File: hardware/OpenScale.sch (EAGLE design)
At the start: 64 parts, among them Q1 200mA/50V, Q2 200mA/50V, Q3 MMBT4403, U1 HX711, U3 TMP102, U4 ATMEGA328P_TQFP, U6 FT231X, Y2 16MHZ

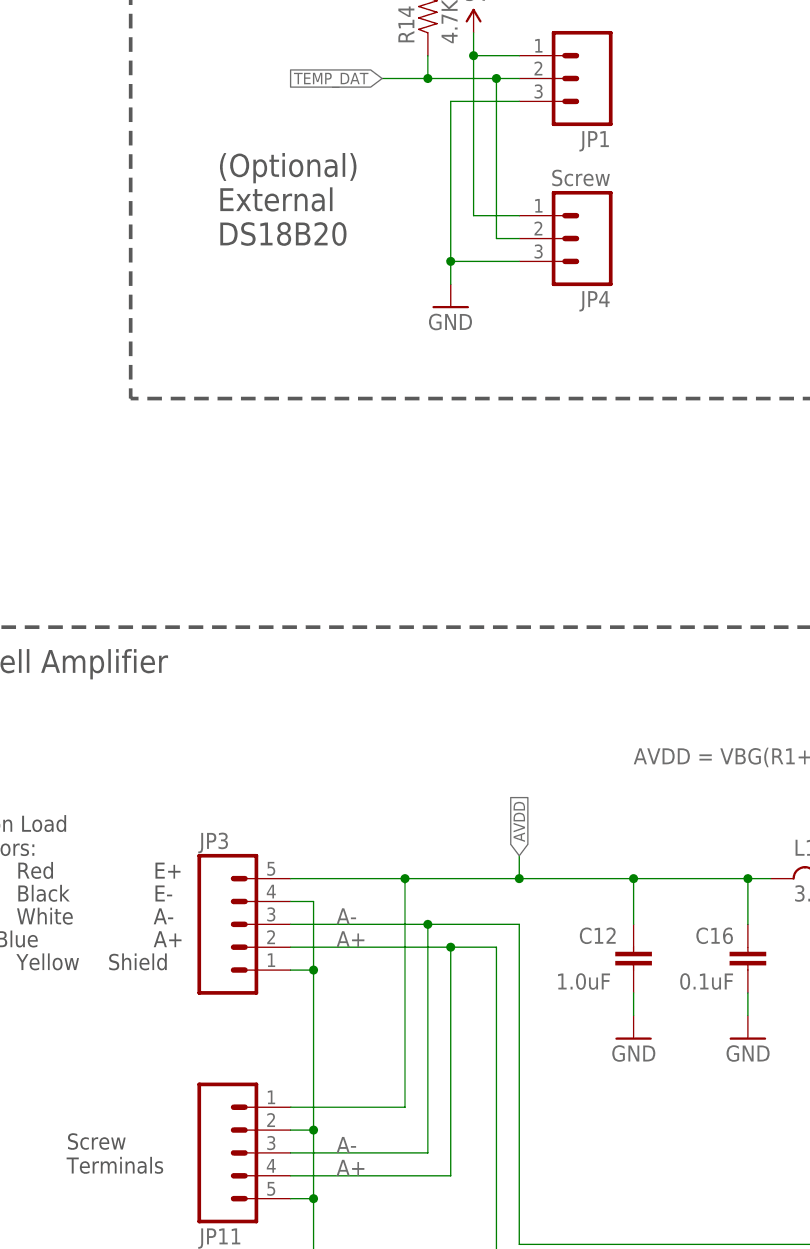
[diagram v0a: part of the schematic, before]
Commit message: Value Additions to .brd and .sch for 3D Model
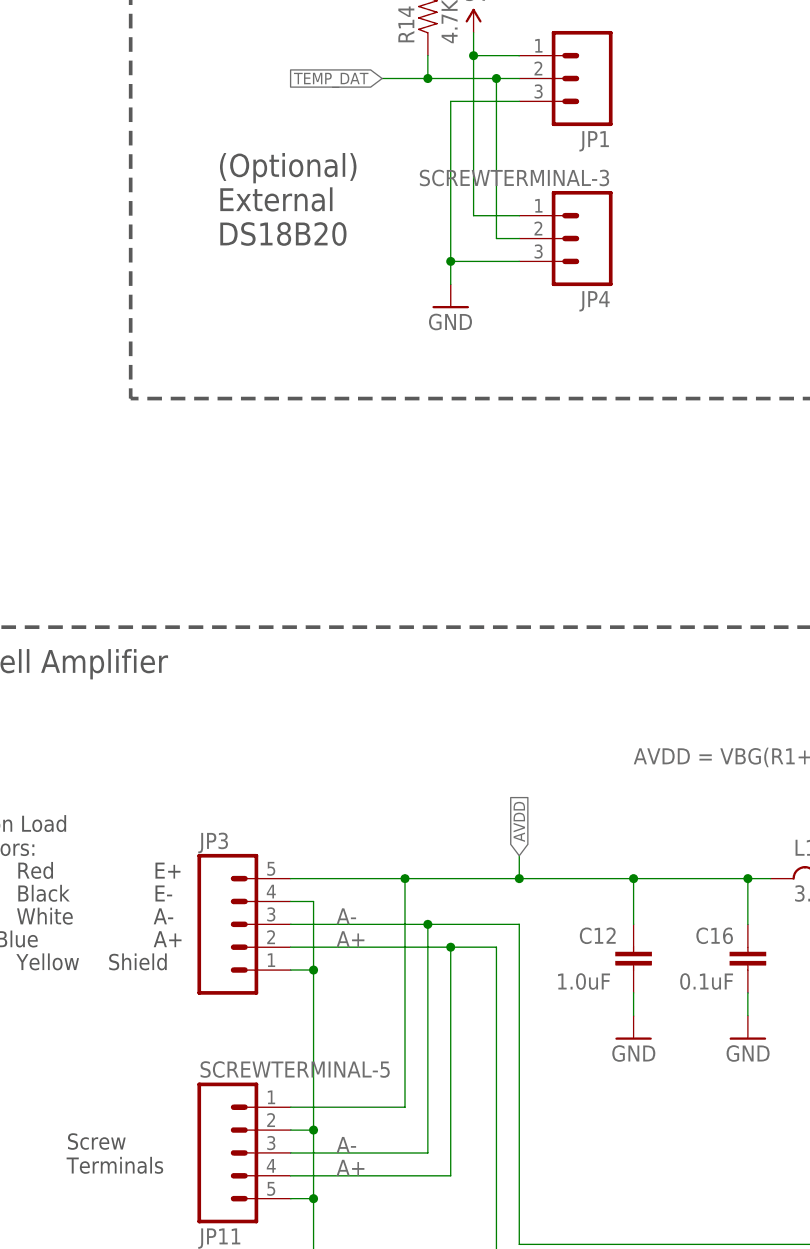
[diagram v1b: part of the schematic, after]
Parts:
- JP11: value (none) -> SCREWTERMINAL-5
- JP4: value Screw -> SCREWTERMINAL-3
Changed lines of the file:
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@@
 <?xml version="1.0" encoding="utf-8"?>
 <!DOCTYPE eagle SYSTEM "eagle.dtd">
-<eagle version="7.1.0">
+<eagle version="7.2.0">
 <drawing>
 <settings>
@@
 <part name="GND20" library="SparkFun-Aesthetics" deviceset="GND" device=""/>
 <part name="LOGO3" library="SparkFun-Aesthetics" deviceset="SFE_LOGO_FLAME" device=".1_STOP" value="SFE_LOGO_FLAME.1_STOP"/>
-<part name="JP4" library="SparkFun-Connectors" deviceset="M03" device="SCREW_LOCK" value="Screw"/>
+<part name="JP4" library="SparkFun-Connectors" deviceset="M03" device="SCREW_LOCK" value="SCREWTERMINAL-3"/>
 <part name="JP3" library="SparkFun-Connectors" deviceset="M05" device="NO_SILK"/>
-<part name="JP11" library="SparkFun-Connectors" deviceset="M05" device="SCREW"/>
+<part name="JP11" library="SparkFun-Connectors" deviceset="M05" device="SCREW" value="SCREWTERMINAL-5"/>
 <part name="L1" library="SparkFun-Passives" deviceset="INDUCTOR" device="0805" value="3.3uH"/>
 </parts>
